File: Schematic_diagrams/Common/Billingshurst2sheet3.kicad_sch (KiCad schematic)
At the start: 0 parts

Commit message: updates to rev B
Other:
- company: Amberley Museum - Billingshurst Signal Box -> Amerley Museum - Billingshurst Signalbox
- title: 8-Channel Relay Module -> Track Diagram Lamp Controller
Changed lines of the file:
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@@
 	(paper "A4")
 	(title_block
-		(title "8-Channel Relay Module")
-		(date "2026-02-09")
-		(rev "A")
-		(company "Amberley Museum - Billingshurst Signal Box")
+		(title "Track Diagram Lamp Controller")
+		(date "07/02/2026")
+		(rev "B")
+		(company "Amerley Museum - Billingshurst Signalbox")
 	)
 	(wire
@@
 				)
 			)
-			(project "Billingshurst 2.2"
+			(project "BT_controller"
 				(path "/5f14c763-48ee-4edd-bd2c-b1ef0de7486e/3be750ae-bd62-458d-aa45-e8d8319abdd3"
 					(page "14")
@@
 				)
 			)
-			(project "Billingshurst 2.2"
+			(project "BT_controller"
 				(path "/5f14c763-48ee-4edd-bd2c-b1ef0de7486e/a9296395-97e1-4ed7-9e45-8211c3011a03"
 					(page "10")
@@
 				)
 			)
-			(project "Billingshurst 2.2"
+			(project "BT_controller"
 				(path "/5f14c763-48ee-4edd-bd2c-b1ef0de7486e/3be750ae-bd62-458d-aa45-e8d8319abdd3"
 					(page "3")
@@
 				)
 			)
-			(project "Billingshurst 2.2"
+			(project "BT_controller"
 				(path "/5f14c763-48ee-4edd-bd2c-b1ef0de7486e/a9296395-97e1-4ed7-9e45-8211c3011a03"
 					(page "6")
@@
 				)
 			)
-			(project "Billingshurst 2.2"
+			(project "BT_controller"
 				(path "/5f14c763-48ee-4edd-bd2c-b1ef0de7486e/3be750ae-bd62-458d-aa45-e8d8319abdd3"
 					(page "16")
@@
 				)
 			)
-			(project "Billingshurst 2.2"
+			(project "BT_controller"
 				(path "/5f14c763-48ee-4edd-bd2c-b1ef0de7486e/a9296395-97e1-4ed7-9e45-8211c3011a03"
 					(page "18")
@@
 				)
 			)
-			(project "Billingshurst 2.2"
+			(project "BT_controller"
 				(path "/5f14c763-48ee-4edd-bd2c-b1ef0de7486e/3be750ae-bd62-458d-aa45-e8d8319abdd3"
 					(page "13")
@@
 				)
 			)
-			(project "Billingshurst 2.2"
+			(project "BT_controller"
 				(path "/5f14c763-48ee-4edd-bd2c-b1ef0de7486e/a9296395-97e1-4ed7-9e45-8211c3011a03"
 					(page "9")
@@
 				)
 			)
-			(project "Billingshurst 2.2"
+			(project "BT_controller"
 				(path "/5f14c763-48ee-4edd-bd2c-b1ef0de7486e/3be750ae-bd62-458d-aa45-e8d8319abdd3"
 					(page "12")
@@
 				)
 			)
-			(project "Billingshurst 2.2"
+			(project "BT_controller"
 				(path "/5f14c763-48ee-4edd-bd2c-b1ef0de7486e/a9296395-97e1-4ed7-9e45-8211c3011a03"
 					(page "8")
@@
 				)
 			)
-			(project "Billingshurst 2.2"
+			(project "BT_controller"
 				(path "/5f14c763-48ee-4edd-bd2c-b1ef0de7486e/3be750ae-bd62-458d-aa45-e8d8319abdd3"
 					(page "15")
@@
 				)
 			)
-			(project "Billingshurst 2.2"
+			(project "BT_controller"
 				(path "/5f14c763-48ee-4edd-bd2c-b1ef0de7486e/a9296395-97e1-4ed7-9e45-8211c3011a03"
 					(page "11")
@@
 				)
 			)
-			(project "Billingshurst 2.2"
+			(project "BT_controller"
 				(path "/5f14c763-48ee-4edd-bd2c-b1ef0de7486e/3be750ae-bd62-458d-aa45-e8d8319abdd3"
 					(page "17")
@@
 				)
 			)
-			(project "Billingshurst 2.2"
+			(project "BT_controller"
 				(path "/5f14c763-48ee-4edd-bd2c-b1ef0de7486e/a9296395-97e1-4ed7-9e45-8211c3011a03"
 					(page "19")
@@
 				)
 			)
-			(project "Billingshurst 2.2"
+			(project "BT_controller"
 				(path "/5f14c763-48ee-4edd-bd2c-b1ef0de7486e/3be750ae-bd62-458d-aa45-e8d8319abdd3"
 					(page "4")
@@
 				)
 			)
-			(project "Billingshurst 2.2"
+			(project "BT_controller"
 				(path "/5f14c763-48ee-4edd-bd2c-b1ef0de7486e/a9296395-97e1-4ed7-9e45-8211c3011a03"
 					(page "7")

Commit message: Amberley spelling corrected
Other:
- company: Amerley Museum - Billingshurst Signalbox -> Amberley Museum - Billingshurst Signalbox
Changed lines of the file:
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@@
 		(date "07/02/2026")
 		(rev "B")
-		(company "Amerley Museum - Billingshurst Signalbox")
+		(company "Amberley Museum - Billingshurst Signalbox")
 	)
 	(wire

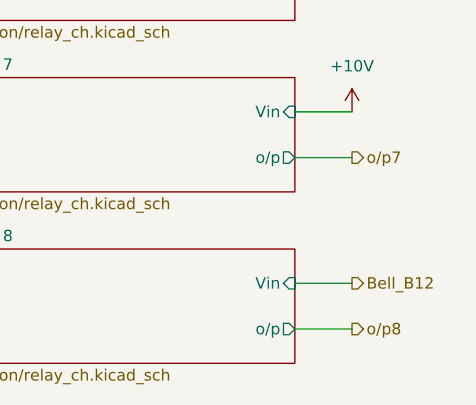
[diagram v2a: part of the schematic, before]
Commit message: internal signal trial
trial was abandoned (inconsistent operation of interrupt)
though some changes were made to wiring and delays
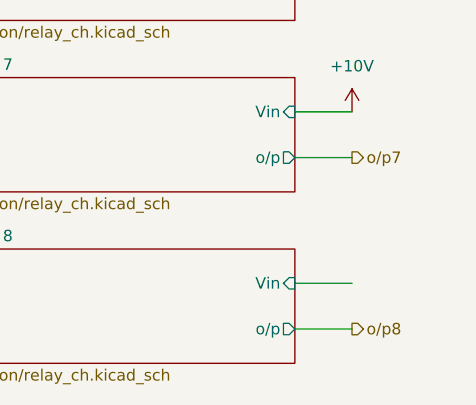
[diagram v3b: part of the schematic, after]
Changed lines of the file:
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@@
-		)
-	)
-	(hierarchical_label "Bell_B12"
-		(shape output)
-		(at 209.55 92.71 0)
-		(effects
-			(font
-				(size 1.27 1.27)
-			)
-			(justify left)
 		)
 	)
